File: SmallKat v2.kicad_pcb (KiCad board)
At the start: 2 copper layers, 90 x 56 mm, 79 parts, among them IC1 TPS562201DDCR, J1 Conn_01x06_Male, J10 Conn_01x03_Male, J11 Conn_01x03_Male, J12 Conn_01x03_Male, J13 Conn_01x03_Male, J14 Conn_01x03_Male, J15 Conn_01x03_Male, J16 Conn_01x03_Male, J17 Conn_01x03_Male, J18 Conn_01x03_Male, J19 Conn_01x03_Male, J2 Conn_01x06_Male, J20 Conn_01x03_Male, J21 Conn_01x02_Male, J3 Conn_01x06_Male, J4 Conn_01x06_Male, J5 Conn_01x03_Male, J6 Conn_01x03_Male, J7 Conn_01x03_Male, J8 Conn_01x03_Male, J9 Conn_01x03_Male, U1 ESP32-DEVKITC-32D, U2 TPS56221, U3 PCA9685BS, U4 BNO055, Y1 32.768kHz

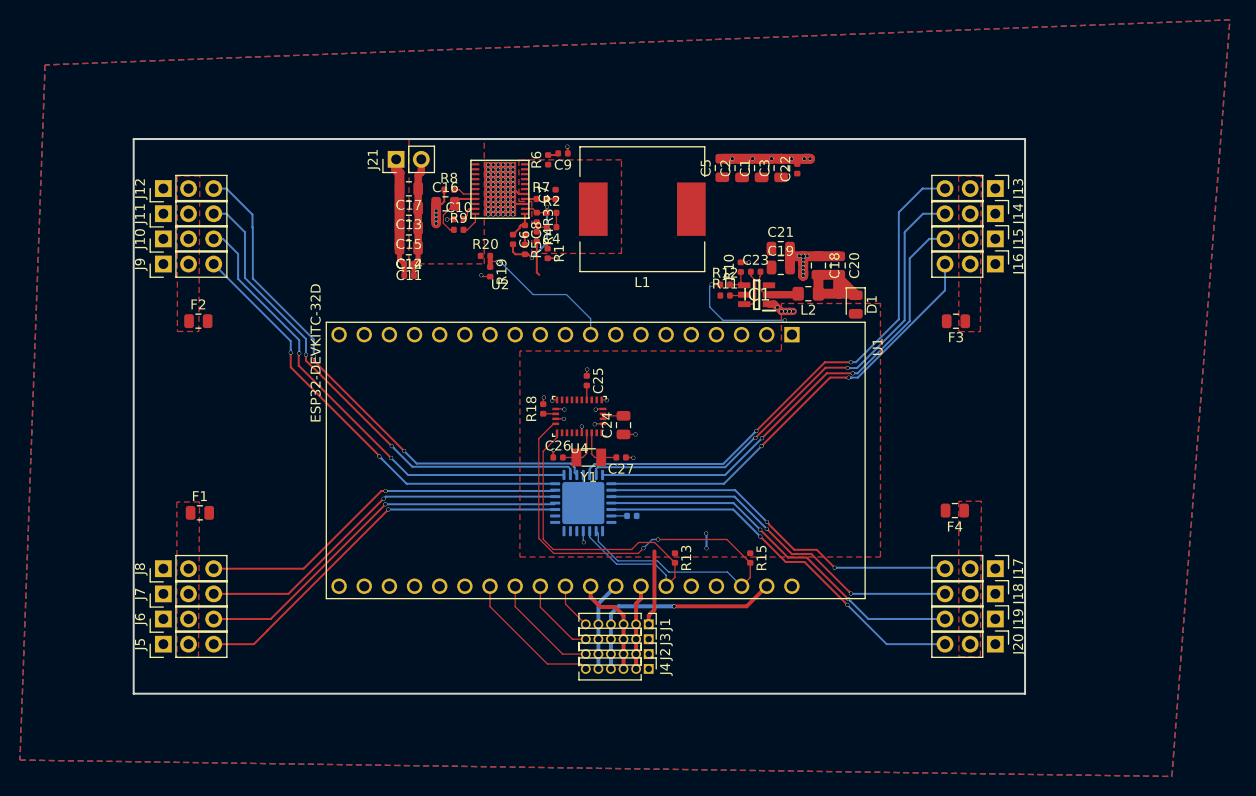
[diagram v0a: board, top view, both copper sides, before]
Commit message: Updated to use BECs and added silkscreen
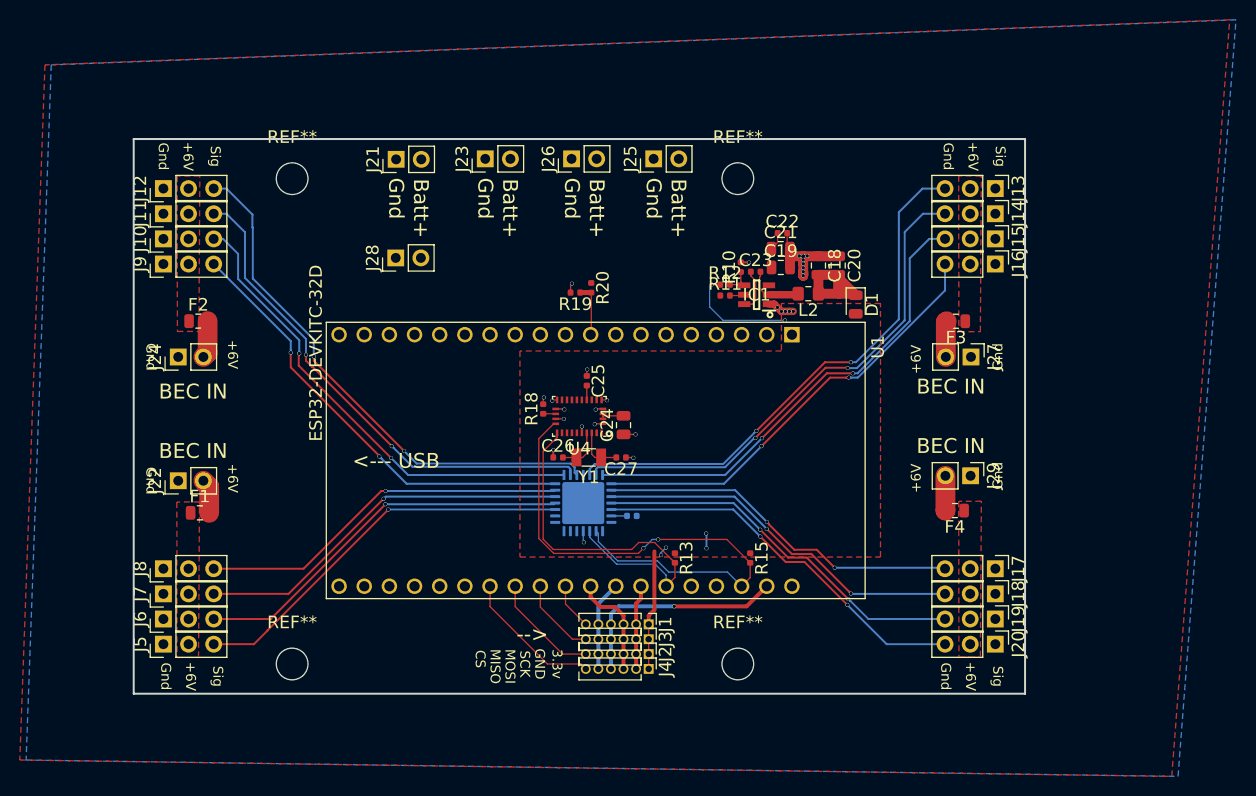
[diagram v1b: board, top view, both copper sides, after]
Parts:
- removed C1, C2, C3, C5: 100uF, Capacitor_SMD:C_0805_2012Metric
- removed C10: 33nF, Capacitor_SMD:C_0402_1005Metric
- removed C11, C14: 1uF, Capacitor_SMD:C_0402_1005Metric
- removed C12, C13, C15, C17: 22uF, Capacitor_SMD:C_0805_2012Metric
- removed C16: 4.7uF, Capacitor_SMD:C_0805_2012Metric
- removed C4: 680pF, Capacitor_SMD:C_0402_1005Metric
- removed C6: 100pF, Capacitor_SMD:C_0402_1005Metric
- removed C7: 100nF, Capacitor_SMD:C_0402_1005Metric
- removed C8: 2200pF, Capacitor_SMD:C_0402_1005Metric
- removed C9: C, Capacitor_SMD:C_0402_1005Metric
- removed L1: 350nH, Inductor_SMD:L_12x12mm_H8mm
- removed R1: 1.1k, Resistor_SMD:R_0402_1005Metric
- removed R2: 1K, Resistor_SMD:R_0402_1005Metric
- removed R3: 10k, Resistor_SMD:R_0402_1005Metric
- removed R4: 50, Resistor_SMD:R_0402_1005Metric
- removed R5: 7.87k, Resistor_SMD:R_0402_1005Metric
- removed R6: 2200pF, Resistor_SMD:R_0402_1005Metric
- removed R7: 5, Resistor_SMD:R_0402_1005Metric
- removed R8: 2K, Resistor_SMD:R_0402_1005Metric
- removed R9: 100k, Resistor_SMD:R_0402_1005Metric
- removed U2: TPS56221, TPS56221:TPS56221
- added J22: Conn_01x02_Male, Connector_PinHeader_2.54mm:PinHeader_1x02_P2.54mm_Vertical, F.Cu at (4.50, 34.5)
- added J23: Conn_01x02_Male, Connector_PinHeader_2.54mm:PinHeader_1x02_P2.54mm_Vertical, F.Cu at (35.5, 2.00)
- added J24: Conn_01x02_Male, Connector_PinHeader_2.54mm:PinHeader_1x02_P2.54mm_Vertical, F.Cu at (4.50, 22.0)
- added J25: Conn_01x02_Male, Connector_PinHeader_2.54mm:PinHeader_1x02_P2.54mm_Vertical, F.Cu at (52.5, 2.00)
- added J26: Conn_01x02_Male, Connector_PinHeader_2.54mm:PinHeader_1x02_P2.54mm_Vertical, F.Cu at (44.2, 2.00)
- added J27: Conn_01x02_Male, Connector_PinHeader_2.54mm:PinHeader_1x02_P2.54mm_Vertical, F.Cu at (84.5, 22.0)
- added J28: Conn_01x02_Male, Connector_PinHeader_2.54mm:PinHeader_1x02_P2.54mm_Vertical, F.Cu at (26.5, 12.0)
- added J29: Conn_01x02_Male, Connector_PinHeader_2.54mm:PinHeader_1x02_P2.54mm_Vertical, F.Cu at (84.5, 34.0)
- added REF**: MountingHole_3.2mm_M3, MountingHole:MountingHole_3.2mm_M3, F.Cu at (61.0, 53.0)
- added REF**: MountingHole_3.2mm_M3, MountingHole:MountingHole_3.2mm_M3, F.Cu at (16.0, 53.0)
- added REF**: MountingHole_3.2mm_M3, MountingHole:MountingHole_3.2mm_M3, F.Cu at (61.0, 4.00)
- added REF**: MountingHole_3.2mm_M3, MountingHole:MountingHole_3.2mm_M3, F.Cu at (16.0, 4.00)
- moved R20 11.2 mm to (46.2, 15.0), turned to 270 degrees
- moved R19 8.85 mm to (44.6, 15.5), turned to 180 degrees
- moved C22 6.67 mm to (65.5, 9.50), turned to 0 degrees
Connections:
- C19 pad 1: +6V -> +BATT
- C21 pad 1: +6V -> +BATT
- C22 pad 1: +6V -> +BATT
- F1 pad 2: +6V -> +6V_IN1
- F2 pad 2: +6V -> +6V_IN2
- F3 pad 2: +6V -> +6V_IN3
- F4 pad 2: +6V -> +6V_IN4
- IC1 pad 3: +6V -> +BATT
- R11 pad 1: +6V -> +BATT
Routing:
- net GND: track 69.6 -> 36.4 mm, vias 107 -> 28
- net Net-(C6-Pad2): track 12.5 -> 0.00 mm, vias 3 -> 0
- net +BATT: track 12.1 -> 1.82 mm
- net BATTMONITOR: track 15.3 -> 5.39 mm, vias 1 -> 0
- net BP: track 6.07 -> 0.00 mm
- net +3V3: track 24.2 -> 29.7 mm, vias 5 -> 7
- net +6V_IN2: track 0.00 -> 3.79 mm
- net +6V_IN3: track 0.00 -> 3.64 mm
- net +6V_IN4: track 0.00 -> 3.52 mm
- net +6V: track 3.49 -> 0.00 mm
- net +6V_IN1: track 0.00 -> 3.48 mm
- net Net-(C6-Pad1): track 2.84 -> 0.00 mm
- net Net-(R8-Pad2): track 2.35 -> 0.00 mm
- net Net-(R9-Pad2): track 2.34 -> 0.00 mm
- net Net-(C4-Pad2): track 2.00 -> 0.00 mm
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- removed copper zone on F.Cu, net +6V
- removed copper zone on F.Cu, net Net-(C7-Pad2)
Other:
- board text added: "+6V"
- board text added: "-->"
- board text added: "3.3v"
- board text added: "<--- USB"
- board text added: "BEC IN"
- board text added: "Batt+"
- board text added: "CS"
- board text added: "GND"
- board text added: "Gnd"
- board text added: "MISO"
- board text added: "MOSI"
- board text added: "Note to Kevin: If you plug something in backwards things will go poof. I have labeled everything as best I can but I cant prevent you from plugging in things backwards so its up to you now -Keion"
- board text added: "SCK"
- board text added: "Sig"
- board text added: "SmallKat V2 Motherboard Rev 2. Keion Bisland Feb. 2019"

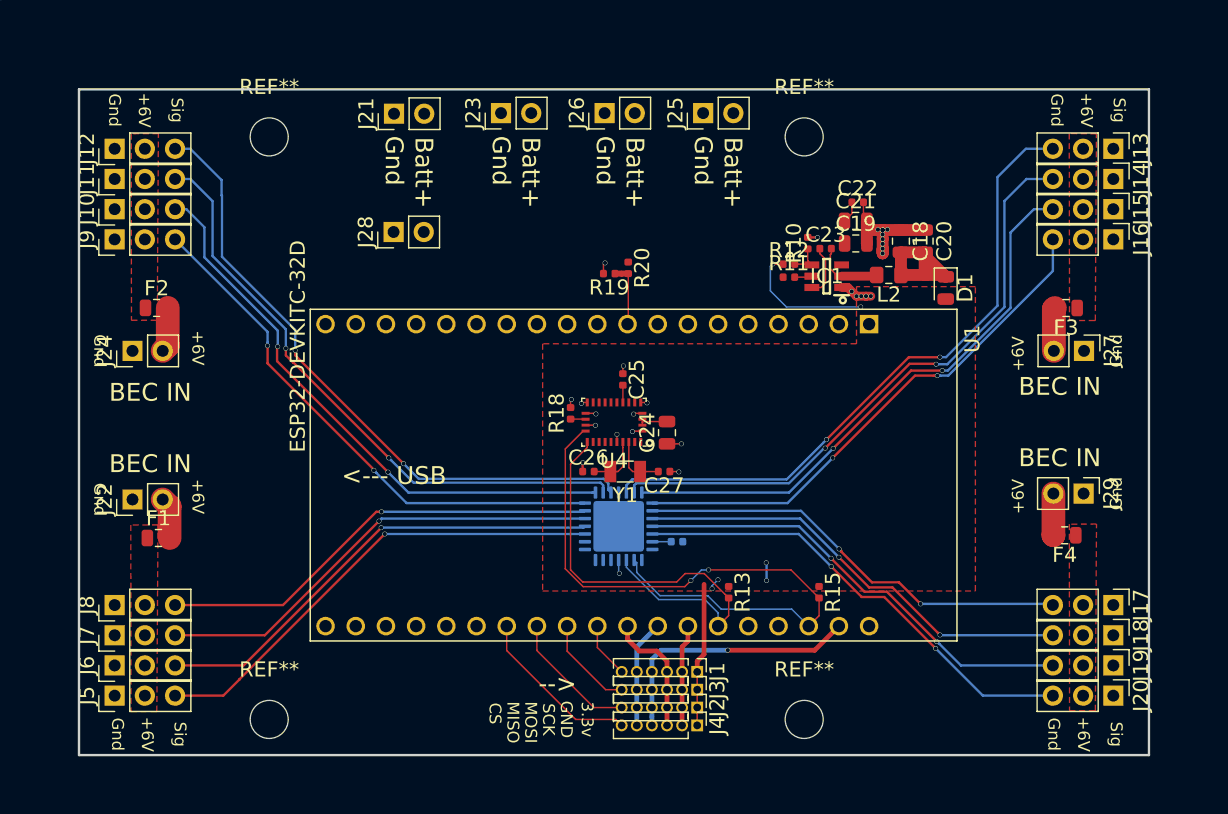
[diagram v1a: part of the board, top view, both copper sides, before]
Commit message: Updated to use nucleo l432kc
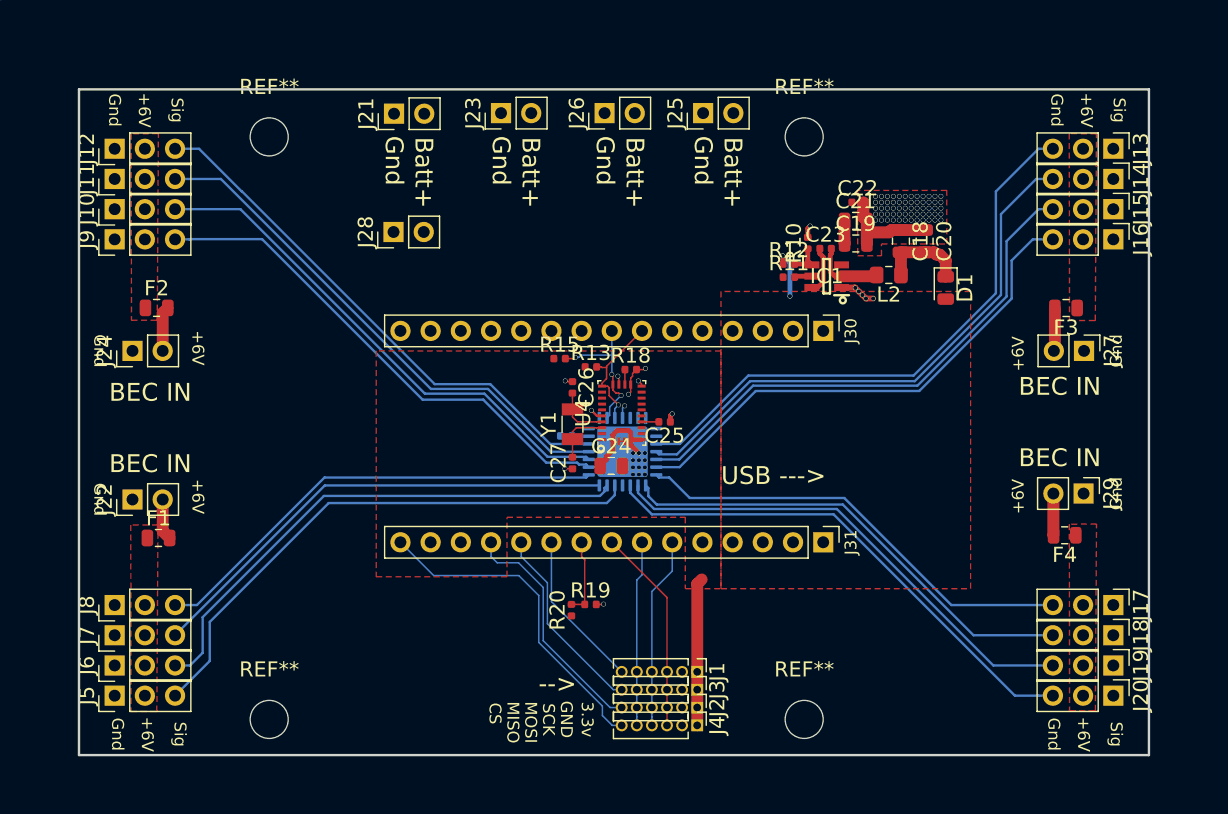
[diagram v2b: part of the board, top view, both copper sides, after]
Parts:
- removed U1: ESP32-DEVKITC-32D, ESP32-DEVKITC-32D:MODULE_ESP32-DEVKITC-32D
- added J30: Conn_01x15_Female, Connector_PinHeader_2.54mm:PinHeader_1x15_P2.54mm_Vertical, F.Cu at (62.6, 20.3)
- added J31: Conn_01x15_Female, Connector_PinHeader_2.54mm:PinHeader_1x15_P2.54mm_Vertical, F.Cu at (62.6, 38.1)
- R12: value 39.5k -> 61.63k
- moved R15 29.4 mm to (40.4, 22.6), turned to 0 degrees
- moved R20 29.2 mm to (41.4, 43.8), turned to 90 degrees
- moved R19 27.9 mm to (43.0, 43.3), turned to 0 degrees
- moved R13 22.2 mm to (43.1, 23.4), turned to 0 degrees
- moved R14 12.9 mm to (41.0, 29.1), turned to 180 degrees
- moved C27 7.74 mm to (41.5, 31.4), turned to 90 degrees
- moved C26 7.21 mm to (41.5, 25.1), turned to 270 degrees
- moved U3 6.28 mm to (45.7, 30.5), turned to 180 degrees
- moved R18 6.26 mm to (46.4, 23.6), turned to 0 degrees
- moved Y1 5.96 mm to (41.5, 28.2), turned to 90 degrees
- moved C24 5.45 mm to (44.8, 31.7), turned to 0 degrees
- moved C25 5.01 mm to (49.3, 28.0), turned to 180 degrees
- moved U4 1.02 mm to (45.7, 27.2), turned to 90 degrees
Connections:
- D1 pad 2: +3V3 -> +5V
- R12 pad 1: +3V3 -> +5V
- U3 pad 1: Net-(U3-Pad1) -> (no net)
- U3 pad 10: SERVO7 -> SERVO15
- U3 pad 12: SERVO8 -> SERVO0
- U3 pad 13: SERVO9 -> SERVO1
- U3 pad 14: SERVO10 -> SERVO2
- U3 pad 15: SERVO11 -> SERVO3
- U3 pad 16: SERVO12 -> SERVO4
- U3 pad 17: SERVO13 -> SERVO5
- U3 pad 18: SERVO14 -> SERVO6
- U3 pad 19: SERVO15 -> SERVO7
- U3 pad 2: Net-(U3-Pad2) -> (no net)
- U3 pad 21: Net-(U3-Pad21) -> (no net)
- U3 pad 26: Net-(U3-Pad26) -> (no net)
- U3 pad 27: Net-(U3-Pad27) -> (no net)
- U3 pad 28: Net-(U3-Pad28) -> (no net)
- U3 pad 3: SERVO0 -> SERVO8
- U3 pad 4: SERVO1 -> SERVO9
- U3 pad 5: SERVO2 -> SERVO10
- U3 pad 6: SERVO3 -> SERVO11
- U3 pad 7: SERVO4 -> SERVO12
- U3 pad 8: SERVO5 -> SERVO13
- U3 pad 9: SERVO6 -> SERVO14
- U4 pad 1: Net-(U4-Pad1) -> (no net)
- U4 pad 10: Net-(U4-Pad10) -> (no net)
- U4 pad 11: /RESET -> (no net)
- U4 pad 12: Net-(U4-Pad12) -> (no net)
- U4 pad 13: Net-(U4-Pad13) -> (no net)
- U4 pad 14: /INT -> (no net)
- U4 pad 21: Net-(U4-Pad21) -> (no net)
- U4 pad 22: Net-(U4-Pad22) -> (no net)
- U4 pad 23: Net-(U4-Pad23) -> (no net)
- U4 pad 24: Net-(U4-Pad24) -> (no net)
- U4 pad 7: Net-(U4-Pad7) -> (no net)
- U4 pad 8: Net-(U4-Pad8) -> (no net)
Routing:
- net SCL: track 56.1 -> 12.3 mm, vias 2 -> 3
- net SDA: track 40.0 -> 10.5 mm, vias 0 -> 1
- net +3V3: track 29.7 -> 14.0 mm, vias 7 -> 1
- net FS4: track 14.3 -> 27.8 mm
- net FS3: track 11.2 -> 20.1 mm
- net SERVO7: track 54.0 -> 45.1 mm, vias 2 -> 0
- net FS1: track 4.70 -> 13.3 mm
- net FS2: track 8.04 -> 16.3 mm
- net GND: track 36.4 -> 28.5 mm, vias 28 -> 87
- net SERVO6: track 51.3 -> 44.3 mm, vias 2 -> 0
- net MOSI: track 22.4 -> 15.6 mm, vias 1 -> 0
- net SCK: track 10.6 -> 17.3 mm
- net SERVO0: track 40.1 -> 46.7 mm, vias 1 -> 0
- net MISO: track 9.08 -> 15.6 mm
- net SERVO8: track 54.5 -> 48.7 mm, vias 2 -> 0
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- added copper zone on F.Cu, net +5V
- added copper zone on F.Cu, net GND
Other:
- board text added: "USB --->"
- board text removed: "<--- USB"

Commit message: init
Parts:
- removed J21, J22, J23, J24, J25, J26, J27, J28, J29: Conn_01x02_Male, Connector_PinHeader_2.54mm:PinHeader_1x02_P2.54mm_Vertical
- removed J30, J31: Conn_01x15_Female, Connector_PinHeader_2.54mm:PinHeader_1x15_P2.54mm_Vertical
- removed REF** (x4): MountingHole_3.2mm_M3, MountingHole:MountingHole_3.2mm_M3
- added BZ1: Buzzer, KLJ-5030:KLJ-5030, F.Cu at (168.9, 117.3)
- added C1: 10uF, Capacitor_SMD:C_0805_2012Metric, F.Cu at (156.7, 108.8)
- added C10: 1000pF, Capacitor_SMD:C_0402_1005Metric, F.Cu at (136.0, 101.9)
- added C11: 100pF, Capacitor_SMD:C_0402_1005Metric, F.Cu at (141.4, 102.9)
- added C12: 10nF, Capacitor_SMD:C_0402_1005Metric, F.Cu at (141.4, 101.5)
- added C13: 1uF, Capacitor_SMD:C_0402_1005Metric, F.Cu at (141.9, 105.5)
- added C14: 4.7uF, Capacitor_SMD:C_0402_1005Metric, F.Cu at (147.7, 105.4)
- added C15: 470nF, Capacitor_SMD:C_0402_1005Metric, F.Cu at (148.0, 102.8)
- added C16: 10uF, Capacitor_SMD:C_1206_3216Metric, F.Cu at (156.8, 104.5)
- added C17: 47uF, Capacitor_SMD:C_1206_3216Metric, F.Cu at (156.8, 96.9)
- added C2: 10uF, Capacitor_SMD:C_0805_2012Metric, F.Cu at (156.7, 106.8)
- added C28: 0.1uF, Capacitor_SMD:C_0402_1005Metric, F.Cu at (152.6, 118.1)
- added C29: 0.1uF, Capacitor_SMD:C_0402_1005Metric, F.Cu at (153.1, 120.8)
- added C3: 22uF, Capacitor_SMD:C_0805_2012Metric, F.Cu at (161.6, 109.8)
- added C31: 0.1uF, Capacitor_SMD:C_0402_1005Metric, F.Cu at (141.4, 127.1)
- added C32: 0.1uF, Capacitor_SMD:C_0402_1005Metric, F.Cu at (114.2, 121.8)
- added C33: 10uF, Capacitor_SMD:C_0805_2012Metric, F.Cu at (121.7, 73.6)
- added C34: 10uF, Capacitor_SMD:C_0805_2012Metric, F.Cu at (123.2, 67.0)
- added C35: 1uF, Capacitor_SMD:C_0402_1005Metric, F.Cu at (123.4, 56.4)
- added C36: 22uF, Capacitor_SMD:C_0805_2012Metric, F.Cu at (163.7, 109.8)
- added C37: 1uF, Capacitor_SMD:C_0402_1005Metric, F.Cu at (120.2, 59.0)
- added C38: 0.1uF, Capacitor_SMD:C_0402_1005Metric, F.Cu at (143.1, 57.6)
- added C39: 4.7uF, Capacitor_SMD:C_0402_1005Metric, F.Cu at (142.1, 57.6)
- added C4: 0.1uF, Capacitor_SMD:C_0402_1005Metric, F.Cu at (153.9, 106.9)
- added C40: 0.1uF, Capacitor_SMD:C_0402_1005Metric, F.Cu at (127.5, 57.8)
- added C41: 0.1uF, Capacitor_SMD:C_0402_1005Metric, F.Cu at (127.5, 56.6)
- added C43: 0.1uF, Capacitor_SMD:C_0402_1005Metric, F.Cu at (140.5, 75.3)
- added C44: 0.1uF, Capacitor_SMD:C_0402_1005Metric, F.Cu at (143.3, 60.4)
- added C5: 22uF, Capacitor_SMD:C_0805_2012Metric, F.Cu at (159.6, 109.9)
- added C6: 0.1uF, Capacitor_SMD:C_0402_1005Metric, F.Cu at (152.3, 113.4)
- added C7: 0.1uF, Capacitor_SMD:C_0402_1005Metric, F.Cu at (142.2, 118.0)
- added C8: 10pF, Capacitor_SMD:C_0402_1005Metric, F.Cu at (143.9, 108.8)
- added C9: 10pF, Capacitor_SMD:C_0402_1005Metric, F.Cu at (142.0, 108.8)
- added D10: LED, LED_SMD:LED_0603_1608Metric, F.Cu at (119.2, 70.4)
- added D11: LED, LED_SMD:LED_0603_1608Metric, F.Cu at (127.4, 74.3)
- added D12: LED, LED_SMD:LED_0603_1608Metric, F.Cu at (130.5, 69.3)
- added D13: D_TVS, Diode_SMD:D_SOD-523, F.Cu at (129.3, 45.0)
- added D14: D_Schottky, Diode_SMD:D_SOD-323, F.Cu at (128.7, 55.0)
- added D15: D_TVS, Diode_SMD:D_SOD-523, F.Cu at (134.7, 45.0)
- added D16: D_TVS, Diode_SMD:D_SOD-523, F.Cu at (131.9, 45.0)
- added D17: LED, LED_SMD:LED_0603_1608Metric, F.Cu at (108.5, 134.2)
- added D18: LED, LED_SMD:LED_0603_1608Metric, F.Cu at (101.3, 97.2)
- added D19: LED, LED_SMD:LED_0603_1608Metric, F.Cu at (181.7, 119.7)
- added D2: LED, LED_SMD:LED_0603_1608Metric, F.Cu at (156.2, 92.8)
- added D20: LED, LED_SMD:LED_0603_1608Metric, F.Cu at (184.2, 110.3)
- added D3: LED, LED_SMD:LED_0603_1608Metric, F.Cu at (160.6, 112.7)
- added D4: LED, LED_SMD:LED_0603_1608Metric, F.Cu at (117.1, 100.0)
- added D5: D_TVS, Diode_SMD:D_SOD-523, F.Cu at (164.1, 121.3)
- added D6: D_Schottky, Diode_SMD:D_SOD-323, F.Cu at (153.7, 126.1)
- added D7: D_TVS, Diode_SMD:D_SOD-523, F.Cu at (164.1, 122.8)
- added D8: D_TVS, Diode_SMD:D_SOD-523, F.Cu at (164.1, 124.3)
- added D9: LED, LED_SMD:LED_0603_1608Metric, F.Cu at (162.5, 77.0)
- added H1: MountingHole_Pad, MountingHole:MountingHole_2.7mm_M2.5_Pad_Via, F.Cu at (160.6, 139.5)
- added H2: MountingHole_Pad, MountingHole:MountingHole_2.7mm_M2.5_Pad_Via, F.Cu at (102.6, 139.5)
- added H3: MountingHole_Pad, MountingHole:MountingHole_2.7mm_M2.5_Pad_Via, F.Cu at (160.6, 90.5)
- added H4: MountingHole_Pad, MountingHole:MountingHole_2.7mm_M2.5_Pad_Via, F.Cu at (102.6, 90.5)
- added H5: MountingHole, MountingHole:MountingHole_2.7mm_M2.5, F.Cu at (114.0, 48.9)
- added H6: MountingHole, MountingHole:MountingHole_2.7mm_M2.5, F.Cu at (173.0, 48.9)
- added H7: MountingHole, MountingHole:MountingHole_2.7mm_M2.5, F.Cu at (114.0, 80.9)
- added H8: MountingHole, MountingHole:MountingHole_2.7mm_M2.5, F.Cu at (173.0, 80.9)
- added IC2: TPS40192DRCT, TPS40192DRCT:SON50P300X300X100-11N, F.Cu at (145.0, 103.0)
- added JP1: Jumper_NO_Small, Jumper:SolderJumper-2_P1.3mm_Open_Pad1.0x1.5mm, F.Cu at (124.8, 74.3)
- added L1: 4.7uH, Inductor_SMD:L_0805_2012Metric, F.Cu at (156.6, 111.0)
- added Q1: BUK9M120-100EX, Package_SON:VSON-8_3.3x3.3mm_P0.65mm_NexFET, F.Cu at (150.4, 97.9)
- added Q2: BUK9M120-100EX, Package_SON:VSON-8_3.3x3.3mm_P0.65mm_NexFET, F.Cu at (145.9, 97.9)
- added Q3: MMBT3904, Package_TO_SOT_SMD:SOT-23, F.Cu at (149.2, 127.9)
- added Q4: MMBT3904, Package_TO_SOT_SMD:SOT-23, F.Cu at (149.2, 131.4)
- added Q5: MMBT3904, Package_TO_SOT_SMD:SOT-23, F.Cu at (139.6, 61.8)
- added Q6: MMBT3904, Package_TO_SOT_SMD:SOT-23, F.Cu at (137.0, 65.2)
- added Q7: 2N3905, Package_TO_SOT_SMD:SOT-23, F.Cu at (164.5, 115.1)
- added R1: R, Resistor_SMD:R_0402_1005Metric, F.Cu at (140.7, 124.1)
- added R16: 3.9k, Resistor_SMD:R_0402_1005Metric, F.Cu at (141.4, 104.0)
- added R17: 100k, Resistor_SMD:R_0402_1005Metric, F.Cu at (143.2, 100.1)
- added R2: 10K, Resistor_SMD:R_0402_1005Metric, F.Cu at (139.3, 118.3)
- added R21: 10K, Resistor_SMD:R_0402_1005Metric, F.Cu at (115.3, 134.5)
- added R22: 10K, Resistor_SMD:R_0402_1005Metric, F.Cu at (150.6, 117.3)
- added R23: 20K, Resistor_SMD:R_0402_1005Metric, F.Cu at (150.2, 118.9)
- added R24: 470R, Resistor_SMD:R_0402_1005Metric, F.Cu at (137.2, 121.3)
- added R25: 10K, Resistor_SMD:R_0402_1005Metric, F.Cu at (146.9, 126.5)
- added R26: 10K, Resistor_SMD:R_0402_1005Metric, F.Cu at (146.8, 129.8)
- added R27: 10K, Resistor_SMD:R_0402_1005Metric, F.Cu at (113.7, 120.3)
- added R28: 330R, Resistor_SMD:R_0402_1005Metric, F.Cu at (159.9, 76.9)
- added R29: 10K, Resistor_SMD:R_0402_1005Metric, F.Cu at (164.7, 59.1)
- added R3: 6.2k, Resistor_SMD:R_0402_1005Metric, F.Cu at (139.3, 117.2)
- added R30: 10K, Resistor_SMD:R_0402_1005Metric, F.Cu at (164.7, 64.0)
- added R31: 330R, Resistor_SMD:R_0402_1005Metric, F.Cu at (121.2, 69.8)
- added R32: 10K, Resistor_SMD:R_0402_1005Metric, F.Cu at (126.3, 70.8)
- added R33: 2.5K, Resistor_SMD:R_0402_1005Metric, F.Cu at (124.8, 77.0)
- added R34: 470R, Resistor_SMD:R_0402_1005Metric, F.Cu at (127.4, 71.7)
- added R35: 470R, Resistor_SMD:R_0402_1005Metric, F.Cu at (127.9, 69.3)
- added R36: 10K, Resistor_SMD:R_0402_1005Metric, F.Cu at (142.5, 73.5)
- added R37: 10K, Resistor_SMD:R_0402_1005Metric, F.Cu at (127.1, 59.1)
- added R38: 20K, Resistor_SMD:R_0402_1005Metric, F.Cu at (127.0, 60.1)
- added R39: 470R, Resistor_SMD:R_0402_1005Metric, F.Cu at (134.9, 60.3)
- added R4: 10K, Resistor_SMD:R_0402_1005Metric, F.Cu at (147.3, 113.7)
- added R40: 10K, Resistor_SMD:R_0402_1005Metric, F.Cu at (134.8, 59.1)
- added R41: 10K, Resistor_SMD:R_0402_1005Metric, F.Cu at (134.9, 61.2)
- added R42: 10K, Resistor_SMD:R_0402_1005Metric, F.Cu at (141.8, 59.4)
- added R43: 10K, Resistor_SMD:R_0402_1005Metric, F.Cu at (161.7, 116.0)
- added R44: R, Resistor_SMD:R_0402_1005Metric, F.Cu at (105.9, 134.2)
- added R45: R, Resistor_SMD:R_0402_1005Metric, F.Cu at (101.8, 95.2)
- added R46: R, Resistor_SMD:R_0402_1005Metric, F.Cu at (182.0, 121.0)
- added R47: R, Resistor_SMD:R_0402_1005Metric, F.Cu at (182.2, 109.8)
- added R5: 10K, Resistor_SMD:R_0402_1005Metric, F.Cu at (146.8, 112.2)
- added R6: 4.7K, Resistor_SMD:R_0402_1005Metric, F.Cu at (156.2, 90.2)
- added R7: 330R, Resistor_SMD:R_0402_1005Metric, F.Cu at (163.1, 112.7)
- added R8: 10K, Resistor_SMD:R_0402_1005Metric, F.Cu at (149.2, 109.0)
- added R9: 33.2K, Resistor_SMD:R_0402_1005Metric, F.Cu at (149.2, 110.0)
- added SW1: SW_SPST, Button_Switch_SMD:SW_SPST_CK_KXT3, F.Cu at (141.2, 132.9)
- added SW2: SW_SPST, Button_Switch_SMD:SW_SPST_CK_KXT3, F.Cu at (141.2, 129.4)
- added SW3: SW_SPST, Button_Switch_SMD:SW_SPST_CK_KXT3, F.Cu at (140.3, 81.2)
- added SW4: SW_SPST, Button_Switch_SMD:SW_SPST_CK_KXT3, F.Cu at (140.3, 77.7)
- added TP1: TestPoint, TestPoint:TestPoint_Pad_D2.5mm, B.Cu at (132.3, 130.7)
- added TP10: TestPoint, TestPoint:TestPoint_Pad_D2.5mm, B.Cu at (126.8, 130.8)
- added TP11: TestPoint, TestPoint:TestPoint_Pad_D2.5mm, B.Cu at (152.1, 127.1)
- added TP12: TestPoint, TestPoint:TestPoint_Pad_D2.5mm, B.Cu at (145.6, 133.2)
- added TP13: TestPoint, TestPoint:TestPoint_Pad_D2.5mm, B.Cu at (152.3, 57.8)
- added TP14: TestPoint, TestPoint:TestPoint_Pad_D2.5mm, B.Cu at (155.9, 57.7)
- added TP15: TestPoint, TestPoint:TestPoint_Pad_D2.5mm, B.Cu at (132.1, 64.9)
- added TP16: TestPoint, TestPoint:TestPoint_Pad_D2.5mm, B.Cu at (141.9, 65.7)
- added TP17: TestPoint, TestPoint:TestPoint_Pad_D2.5mm, B.Cu at (116.1, 73.2)
- added TP18: TestPoint, TestPoint:TestPoint_Pad_D2.5mm, B.Cu at (133.3, 79.5)
- added TP19: TestPoint, TestPoint:TestPoint_Pad_D2.5mm, B.Cu at (159.0, 68.8)
- added TP2: TestPoint, TestPoint:TestPoint_Pad_D2.5mm, B.Cu at (146.5, 109.0)
- added TP3: TestPoint, TestPoint:TestPoint_Pad_D2.5mm, B.Cu at (149.6, 114.2)
- added TP4: TestPoint, TestPoint:TestPoint_Pad_D2.5mm, B.Cu at (129.7, 123.8)
- added TP5: TestPoint, TestPoint:TestPoint_Pad_D2.5mm, B.Cu at (166.2, 109.3)
- added TP6: TestPoint, TestPoint:TestPoint_Pad_D2.5mm, B.Cu at (156.1, 88.8)
- added TP7: TestPoint, TestPoint:TestPoint_Pad_D2.5mm, B.Cu at (140.0, 91.7)
- added TP8: TestPoint, TestPoint:TestPoint_Pad_D2.5mm, B.Cu at (116.6, 95.1)
- added TP9: TestPoint, TestPoint:TestPoint_Pad_D2.5mm, B.Cu at (123.0, 130.9)
- added U1: BNO055, Package_LGA:LGA-28_5.2x3.8mm_P0.5mm, F.Cu at (143.6, 115.0)
- added U2: MIC5365-3.3YC5, Package_TO_SOT_SMD:SOT-23-5, F.Cu at (152.7, 130.9)
- added U5: MCP73831-2-OT, Package_TO_SOT_SMD:SOT-23-5, F.Cu at (123.8, 70.5)
- added U6: MIC5365-3.3YC5, Package_TO_SOT_SMD:SOT-23-5, F.Cu at (123.0, 58.8)
- added U7: ESP32-WROOM-32, RF_Module:ESP32-WROOM-32, F.Cu at (153.7, 65.2)
- added U8: CP2102N-A01-GQFN24, Package_DFN_QFN:QFN-24-1EP_4x4mm_P0.5mm_EP2.6x2.6mm, F.Cu at (131.1, 59.9)
- added U9: WIICHUCK, WIICHUCK:CHUCK, F.Cu at (169.5, 61.8)
- C18: value 22uF -> 10uF; footprint Capacitor_SMD:C_0805_2012Metric -> Capacitor_SMD:C_1206_3216Metric
- C19: value 10Uf -> 100uF; footprint Capacitor_SMD:C_0805_2012Metric -> Capacitor_SMD:C_1210_3225Metric
- C20: value 22uF -> 47uF; footprint Capacitor_SMD:C_0805_2012Metric -> Capacitor_SMD:C_1206_3216Metric
- C21: value 10uF -> 100uF; footprint Capacitor_SMD:C_0805_2012Metric -> Capacitor_SMD:C_1210_3225Metric
- C22, C23, C25: value 0.1uF -> 1uF
- C24: value 10uF -> 22uF
- C26: value 10pF -> 0.1uF
- C27: value 10pF -> 4.7uF
- D1: value DIODE -> LED; footprint Diode_SMD:D_0805_2012Metric -> LED_SMD:LED_0603_1608Metric
- F1, F2, F3, F4: footprint Fuse:Fuse_0805_2012Metric -> 01550900M:0154.250DR
- J1, J2, J3, J4: value Conn_01x06_Male -> Conn_01x03_Male; footprint Connector_PinHeader_1.27mm:PinHeader_1x06_P1.27mm_Vertical -> Connector_PinHeader_2.54mm:PinHeader_1x03_P2.54mm_Vertical
- J18: value Conn_01x03_Male -> Conn_01x02_Male; footprint Connector_PinHeader_2.54mm:PinHeader_1x03_P2.54mm_Vertical -> Connector_JST:JST_PH_S2B-PH-K_1x02_P2.00mm_Horizontal
- J19, J20: value Conn_01x03_Male -> USB_C_Receptacle; footprint Connector_PinHeader_2.54mm:PinHeader_1x03_P2.54mm_Vertical -> U263-241N-4BQC11-1:U263241N4BQC111
- J9: value Conn_01x03_Male -> Conn_01x02_Male; footprint Connector_PinHeader_2.54mm:PinHeader_1x03_P2.54mm_Vertical -> SmallKat ESP32:SHDR2W320P716_1X2_1574X813X1588P
- L2: value 4.7uH -> 1uH; footprint Inductor_SMD:L_0805_2012Metric_Pad1.15x1.40mm_HandSolder -> Inductor_SMD:L_Bourns_SRP1245A
- R12: value 61.63k -> 2.18k
- R13: value 10K -> 20k
- R14: value 10K -> 2.61k; moved to F.Cu
- R15: value 10K -> 4.22k
- R18, R19: value 10K -> 100k
- R20: value 6.2k -> 1K
- U3: value PCA9685BS -> ESP32-WROOM-32; footprint Package_DFN_QFN:QFN-28-1EP_6x6mm_P0.65mm_EP4.25x4.25mm -> RF_Module:ESP32-WROOM-32; moved to F.Cu
- U4: value BNO055 -> CP2102N-A01-GQFN24; footprint Package_LGA:LGA-28_5.2x3.8mm_P0.5mm -> Package_DFN_QFN:QFN-24-1EP_4x4mm_P0.5mm_EP2.6x2.6mm
- moved J10 217.8 mm to (184.1, 131.2), turned to 270 degrees
- moved J11 217.8 mm to (184.1, 128.7), turned to 270 degrees
- moved J12 217.8 mm to (184.1, 126.1), turned to 270 degrees
- moved J9 163.1 mm to (145.8, 91.5), turned to 0 degrees
- moved J13 153.2 mm to (184.1, 123.6)
- moved F3 151.5 mm to (178.7, 135.8)
- moved C25 147.9 mm to (152.8, 133.5)
- moved C23 146.3 mm to (153.1, 128.4), turned to 180 degrees
- moved C27 141.6 mm to (152.6, 119.2), turned to 0 degrees
- moved U4 141.2 mm to (149.9, 122.6), turned to 180 degrees
- moved J14 135.0 mm to (184.0, 101.3)
- moved R11 132.9 mm to (147.3, 115.7), turned to 270 degrees
- moved R10 131.7 mm to (149.2, 111.0), turned to 0 degrees
- moved J15 131.5 mm to (184.1, 98.8)
- moved Y1 130.8 mm to (143.0, 110.7), turned to 0 degrees
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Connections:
- C18 pad 1: GND -> +BATT
- C18 pad 2: Net-(C18-Pad2) -> GND
- C19 pad 1: +BATT -> +6V
- C20 pad 1: GND -> +BATT
- C20 pad 2: Net-(C18-Pad2) -> GND
- C21 pad 1: +BATT -> +6V
- C22 pad 1: +BATT -> +6V
- C23 pad 1: Net-(C23-Pad1) -> +5V
- C23 pad 2: Net-(C23-Pad2) -> GND
- C24 pad 1: GND -> +3V3
- C24 pad 2: +3V3 -> GND
- C25 pad 1: GND -> +3V3
- C25 pad 2: Net-(C25-Pad2) -> GND
- C26 pad 1: GND -> +3V3
- C26 pad 2: Net-(C26-Pad2) -> GND
- C27 pad 1: GND -> +3V3
- C27 pad 2: Net-(C27-Pad2) -> GND
- D1 pad 1: Net-(C18-Pad2) -> GND
- D1 pad 2: +5V -> Net-(D1-Pad2)
- F1 pad 1: +6V_1 -> Net-(F1-Pad1)
- F1 pad 2: +6V_IN1 -> +6V
- F2 pad 1: +6V_2 -> Net-(F2-Pad1)
- F2 pad 2: +6V_IN2 -> +6V
- F3 pad 1: +6V_3 -> Net-(F3-Pad1)
- F3 pad 2: +6V_IN3 -> +6V
- F4 pad 1: +6V_4 -> Net-(F4-Pad1)
- F4 pad 2: +6V_IN4 -> +6V
- IC1 pad 2: Net-(C23-Pad2) -> Net-(C6-Pad2)
- IC1 pad 6: Net-(C23-Pad1) -> Net-(C6-Pad1)
- J1 pad 1: +3V3 -> GND
- J1 pad 2: GND -> Net-(F1-Pad1)
- J1 pad 3: SCK -> /MainBoard/SERVO0
- J10 pad 2: +6V_2 -> Net-(F3-Pad1)
- J10 pad 3: SERVO5 -> /MainBoard/SERVO8
- J11 pad 2: +6V_2 -> Net-(F3-Pad1)
- J11 pad 3: SERVO6 -> /MainBoard/SERVO9
- J12 pad 2: +6V_2 -> Net-(F3-Pad1)
- J12 pad 3: SERVO7 -> /MainBoard/SERVO10
- J13 pad 2: +6V_3 -> Net-(F3-Pad1)
- J13 pad 3: SERVO8 -> /MainBoard/SERVO11
- J14 pad 2: +6V_3 -> Net-(F4-Pad1)
- J14 pad 3: SERVO9 -> /MainBoard/SERVO12
- J15 pad 2: +6V_3 -> Net-(F4-Pad1)
- J15 pad 3: SERVO10 -> /MainBoard/SERVO13
- J16 pad 2: +6V_3 -> Net-(F4-Pad1)
- J16 pad 3: SERVO11 -> /MainBoard/SERVO14
- J17 pad 2: +6V_4 -> Net-(F4-Pad1)
- J17 pad 3: SERVO12 -> /MainBoard/SERVO15
- J18 pad 2: +6V_4 -> +3V8
- J2 pad 1: +3V3 -> GND
- J2 pad 2: GND -> Net-(F1-Pad1)
- J2 pad 3: SCK -> /MainBoard/SERVO1
- J3 pad 1: +3V3 -> GND
- J3 pad 2: GND -> Net-(F1-Pad1)
- J3 pad 3: SCK -> /MainBoard/SERVO2
- J4 pad 1: +3V3 -> GND
- J4 pad 2: GND -> Net-(F1-Pad1)
- J4 pad 3: SCK -> /MainBoard/SERVO3
- J5 pad 2: +6V_1 -> Net-(F2-Pad1)
- J5 pad 3: SERVO0 -> /MainBoard/SERVO4
- J6 pad 2: +6V_1 -> Net-(F2-Pad1)
- J6 pad 3: SERVO1 -> /MainBoard/SERVO5
- J7 pad 2: +6V_1 -> Net-(F2-Pad1)
- J7 pad 3: SERVO2 -> /MainBoard/SERVO6
- J8 pad 2: +6V_1 -> Net-(F2-Pad1)
- J8 pad 3: SERVO3 -> /MainBoard/SERVO7
- J9 pad 2: +6V_2 -> +BATT
- L2 pad 1: Net-(C18-Pad2) -> Net-(C15-Pad1)
- L2 pad 2: Net-(C23-Pad2) -> +6V
- R10 pad 1: Net-(IC1-Pad4) -> +BATT
- R10 pad 2: GND -> Net-(IC1-Pad5)
- R11 pad 1: +BATT -> Net-(R11-Pad1)
- R11 pad 2: Net-(IC1-Pad5) -> GND
- R12 pad 1: +5V -> Net-(C11-Pad2)
- R12 pad 2: Net-(IC1-Pad4) -> GND
- R13 pad 1: +3V3 -> +6V
- R13 pad 2: SDA -> Net-(C11-Pad2)
- R14 pad 1: Net-(R14-Pad1) -> Net-(C11-Pad2)
- R14 pad 2: GND -> Net-(C10-Pad2)
- R15 pad 1: +3V3 -> Net-(C12-Pad2)
- R15 pad 2: SCL -> Net-(C11-Pad2)
- R18 pad 1: Net-(R18-Pad1) -> Net-(C14-Pad1)
- R18 pad 2: GND -> Net-(IC2-Pad5)
- R19 pad 1: BATTMONITOR -> Net-(C15-Pad1)
- R19 pad 2: GND -> Net-(C15-Pad2)
- R20 pad 1: +BATT -> +6V
- R20 pad 2: BATTMONITOR -> Net-(D4-Pad2)
- U3 pad 1: (no net) -> GND
- U3 pad 10: SERVO15 -> /MainBoard/SERVO4
- U3 pad 11: GND -> /MainBoard/SERVO3
- U3 pad 12: SERVO0 -> /MainBoard/SERVO2
- U3 pad 13: SERVO1 -> /MainBoard/SERVO1
- U3 pad 14: SERVO2 -> /MainBoard/SERVO0
- U3 pad 15: SERVO3 -> GND
- U3 pad 16: SERVO4 -> /MainBoard/SERVO8
- U3 pad 17: SERVO5 -> (no net)
- U3 pad 18: SERVO6 -> (no net)
- U3 pad 19: SERVO7 -> (no net)
- U3 pad 2: (no net) -> +3V3
- U3 pad 20: Net-(R14-Pad1) -> (no net)
- U3 pad 22: GND -> (no net)
- U3 pad 23: SCL -> /MainBoard/SERVO9
- U3 pad 24: SDA -> /MainBoard/SERVO10
- U3 pad 25: +3V3 -> /MainBoard/ESP32Module/IO0
- U3 pad 26: (no net) -> /MainBoard/SERVO11
- U3 pad 27: (no net) -> /MainBoard/SERVO12
- U3 pad 28: (no net) -> /MainBoard/SERVO13
- U3 pad 29: GND -> /MainBoard/SERVO14
- U3 pad 3: SERVO8 -> /MainBoard/ESP32Module/EN
- U3 pad 4: SERVO9 -> (no net)
- U3 pad 5: SERVO10 -> (no net)
- U3 pad 6: SERVO11 -> (no net)
- U3 pad 7: SERVO12 -> /MainBoard/BATTMONITOR
- U3 pad 8: SERVO13 -> /MainBoard/SERVO6
- U3 pad 9: SERVO14 -> /MainBoard/SERVO5
- U4 pad 15: GND -> (no net)
- U4 pad 16: GND -> (no net)
- U4 pad 17: Net-(R18-Pad1) -> (no net)
- U4 pad 18: GND -> (no net)
- U4 pad 19: SCL -> /MainBoard/ESP32Module/RTS
- U4 pad 20: SDA -> Net-(R24-Pad2)
- U4 pad 21: (no net) -> /MainBoard/ESP32Module/RXD
- U4 pad 23: (no net) -> /MainBoard/ESP32Module/DTR
- U4 pad 3: +3V3 -> /MainBoard/ESP32Module/USBD_P
- U4 pad 4: +3V3 -> /MainBoard/ESP32Module/USBD_N
- U4 pad 5: GND -> +3V3
- U4 pad 6: GND -> +3V3
- U4 pad 7: (no net) -> +3V3
- U4 pad 8: (no net) -> Net-(R22-Pad1)
- U4 pad 9: Net-(C25-Pad2) -> (no net)
- Y1 pad 1: Net-(C26-Pad2) -> Net-(C8-Pad2)
- Y1 pad 2: Net-(C27-Pad2) -> Net-(C9-Pad2)
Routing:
- net GND: track 28.5 -> 125.7 mm, vias 87 -> 315
- net /MainBoard/SERVO8: track 0.00 -> 90.6 mm, vias 0 -> 4
- net /MainBoard/SERVO15: track 0.00 -> 64.5 mm, vias 0 -> 3
- net /MainBoard/SERVO14: track 0.00 -> 62.8 mm, vias 0 -> 3
- net /MainBoard/SERVO13: track 0.00 -> 61.1 mm, vias 0 -> 3
- net /MainBoard/SERVO12: track 0.00 -> 59.7 mm, vias 0 -> 3
- net /MainBoard/SERVO9: track 0.00 -> 53.7 mm, vias 0 -> 1
- net /MainBoard/SERVO10: track 0.00 -> 52.8 mm, vias 0 -> 1
- net /MainBoard/SERVO11: track 0.00 -> 52.8 mm, vias 0 -> 1
- net /MainBoard/SERVO7: track 0.00 -> 52.0 mm, vias 0 -> 1
- net SERVO8: track 48.7 -> 0.00 mm
- net /MainBoard/ESP32Module/EN: track 0.00 -> 47.2 mm, vias 0 -> 2
- net SERVO9: track 47.0 -> 0.00 mm
- net SERVO0: track 46.7 -> 0.00 mm
- net SERVO7: track 45.1 -> 0.00 mm
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- added copper zone on B.Cu, net +6V
- added copper zone on F.Cu, net +6V
- added copper zone on F.Cu, net Net-(C15-Pad1)
- removed copper zone on F.Cu, net +6V_1
- removed copper zone on F.Cu, net +6V_2
- removed copper zone on F.Cu, net +6V_3
- removed copper zone on F.Cu, net +6V_4
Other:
- board size 90 x 56 mm -> 89 x 99 mm
- board text added: "+"
- board text added: "-"
- board text added: "5v"
- board text added: "6v"
- board text added: "BATT IN"
- board text added: "BATT+"
- board text added: "BATT-"
- board text added: "DTR"
- board text added: "EN"
- board text added: "Elbow"
- board text added: "Fuse Good"
- board text added: "Head Pan"
- board text added: "Head Tilt"
- board text added: "IO0"
- board text added: "IO19"
- board text added: "IO2"
- board text added: "Keion Bisland"
- board text added: "Pan"
- board text added: "RTS"
- board text added: "RX"
- board text added: "Rev 1.0"
- board text added: "SCL"
- board text added: "SDA"
- board text added: "SmallKat Mother Board"
- board text added: "SmallKat Remote Controller Board"
- board text added: "TX"
- board text added: "Tail Pan"
- board text added: "Tail Tilt"
- board text added: "Tilt"
- board text removed: "+6V"
- board text removed: "-->"
- board text removed: "BEC IN"
- board text removed: "Batt+"
- board text removed: "CS"
- board text removed: "Gnd"
- board text removed: "MISO"
- board text removed: "MOSI"
- board text removed: "Note to Kevin: If you plug something in backwards things will go poof. I have labeled everything as best I can but I cant prevent you from plugging in things backwards so its up to you now -Keion"
- board text removed: "SCK"
- board text removed: "Sig"
- board text removed: "SmallKat V2 Motherboard Rev 2. Keion Bisland Feb. 2019"
- board text removed: "USB --->"
